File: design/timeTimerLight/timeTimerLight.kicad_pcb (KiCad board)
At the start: 2 copper layers, 1 part

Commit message: Got components layed out on PCB editor, no traces yet.  Switched to right-angle connector.
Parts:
- removed REF**: MCP1640, Package_TO_SOT_SMD:SOT-23-6
- added C1: 10u, customParts:CAPRB250W50L400T250H550, F.Cu at (138.0, 116.0)
- added C2: 10u, customParts:CAPRB250W50L400T250H550, F.Cu at (156.5, 120.5)
- added D1: LED, LED_THT:LED_D5.0mm, F.Cu at (162.5, 135.0)
- added J1: 640455-3, customParts:TE_640455-3, F.Cu at (127.4, 120.3)
- added L1: 4u7, customParts:IND_CDRH2D18_HPNP-4R7NC, F.Cu at (139.5, 128.0)
- added Q1: 2N3906, Package_TO_SOT_THT:TO-92_Inline, F.Cu at (149.1, 115.2)
- added R1: 10k, customParts:RESAD1100W55L630D240B, F.Cu at (138.5, 120.5)
- added R2: 100k, customParts:RESAD1100W55L630D240B, F.Cu at (132.5, 130.5)
- added R3: 976k, customParts:RESAD1100W55L630D240B, F.Cu at (150.0, 126.0)
- added R4: 562k, customParts:RESAD1100W55L630D240B, F.Cu at (150.0, 129.5)
- added R5: 220R, customParts:RESAD1100W55L630D240B, F.Cu at (163.0, 121.0)
- added S1: OS102011MS2QS1, customParts:OS102011MS2QS1, F.Cu at (123.5, 128.6)
- added U1: MCP1640x-xCHY, Package_TO_SOT_SMD:SOT-23-6, F.Cu at (142.0, 134.0)
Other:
- board outline added: 50.8 x 25.4 mm

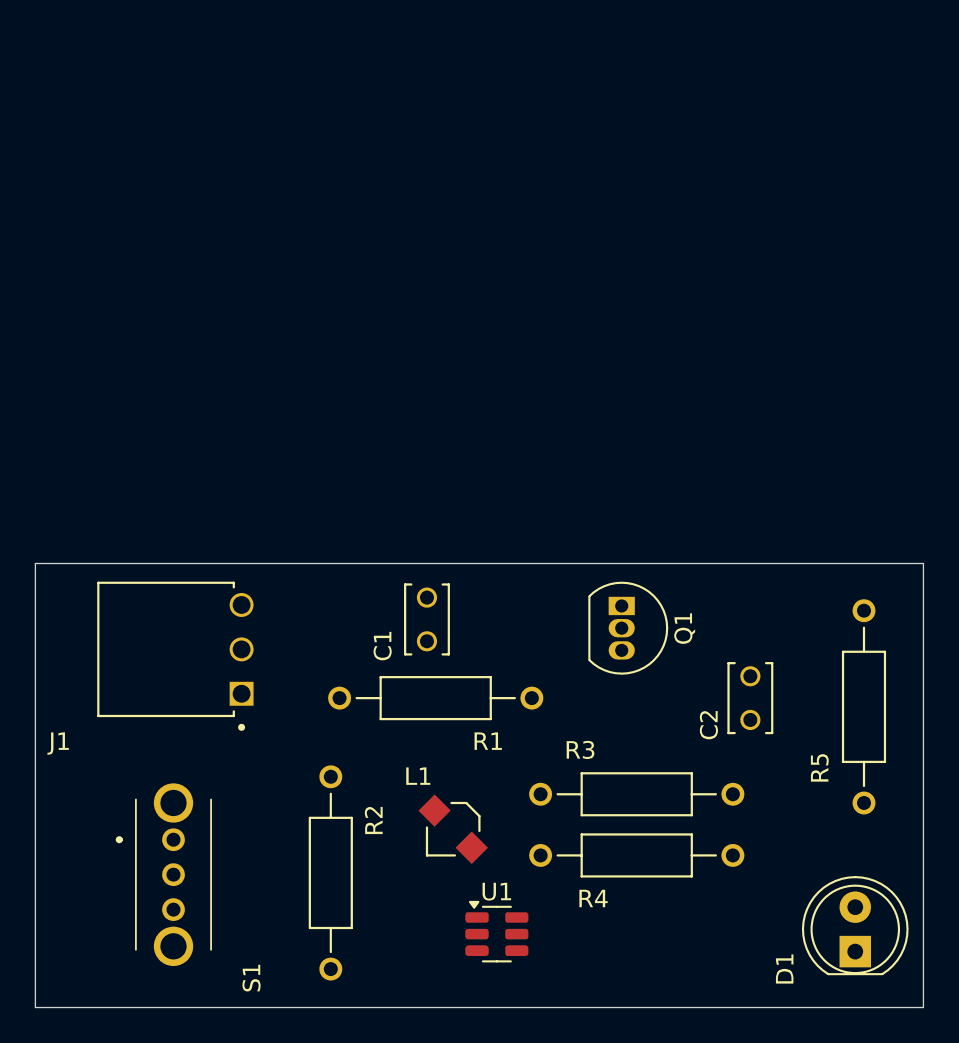
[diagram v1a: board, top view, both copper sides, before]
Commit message: Front traces done.  Still need to do ground plane
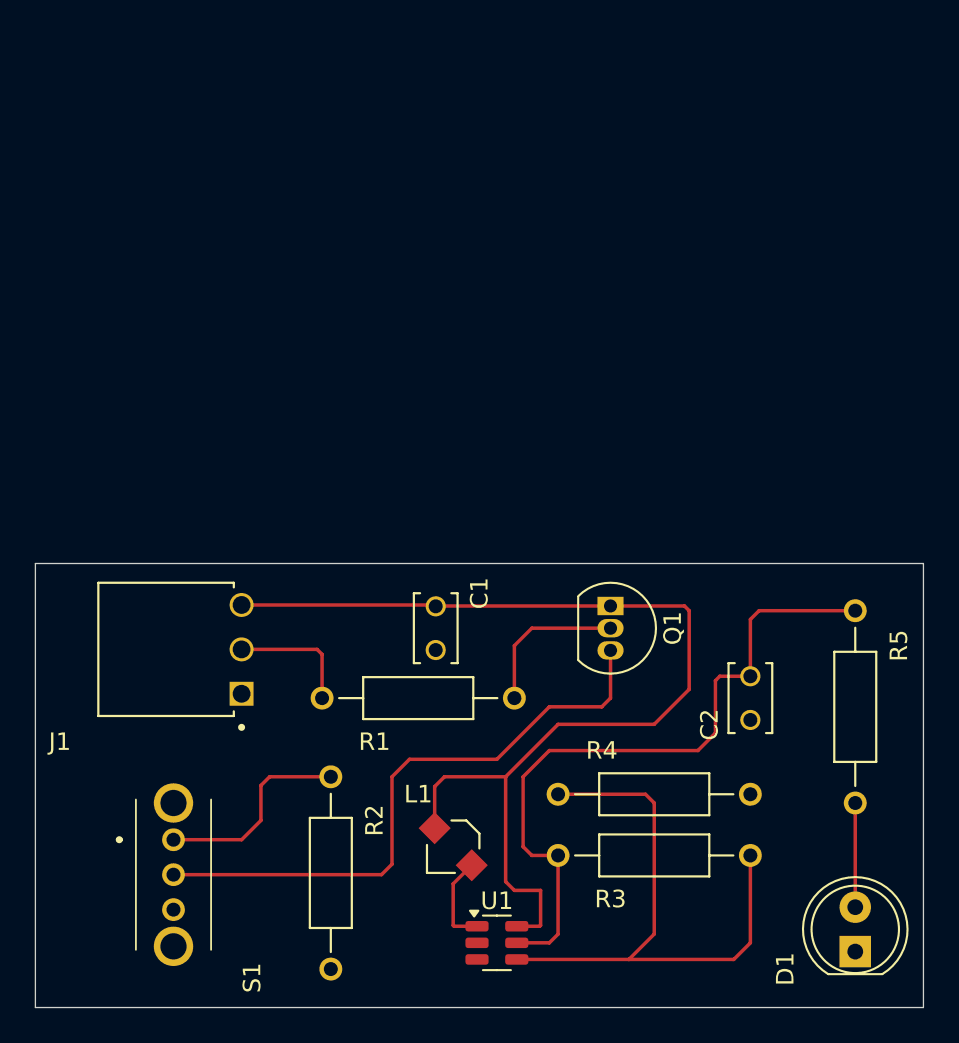
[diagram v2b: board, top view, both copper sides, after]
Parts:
- moved R3 3.64 mm to (151.0, 129.5)
- moved R4 3.64 mm to (151.0, 126.0)
- moved L1 1.00 mm to (139.5, 129.0)
- moved R1 1.00 mm to (137.5, 120.5), turned to 180 degrees
- moved C1 0.71 mm to (138.5, 116.5), turned to -90 degrees
- moved Q1 0.64 mm to (148.5, 115.2)
- moved R5 0.50 mm to (162.5, 121.0), turned to -90 degrees
- moved U1 0.50 mm to (142.0, 134.5)
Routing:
- net /+1V2: track 0.00 -> 61.1 mm
- net GND1: track 0.00 -> 39.9 mm
- net Net-(Q1-C): track 0.00 -> 34.8 mm
- net Net-(U1-V_{FB}): track 0.00 -> 34.0 mm
- net Net-(S1-NO): track 0.00 -> 11.7 mm
- net Net-(Q1-B): track 0.00 -> 8.91 mm
- net /ALARM: track 0.00 -> 7.22 mm
- net Net-(D1-A): track 0.00 -> 5.96 mm
- net Net-(U1-SW): track 0.00 -> 5.26 mm

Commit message: Back ground traces done too
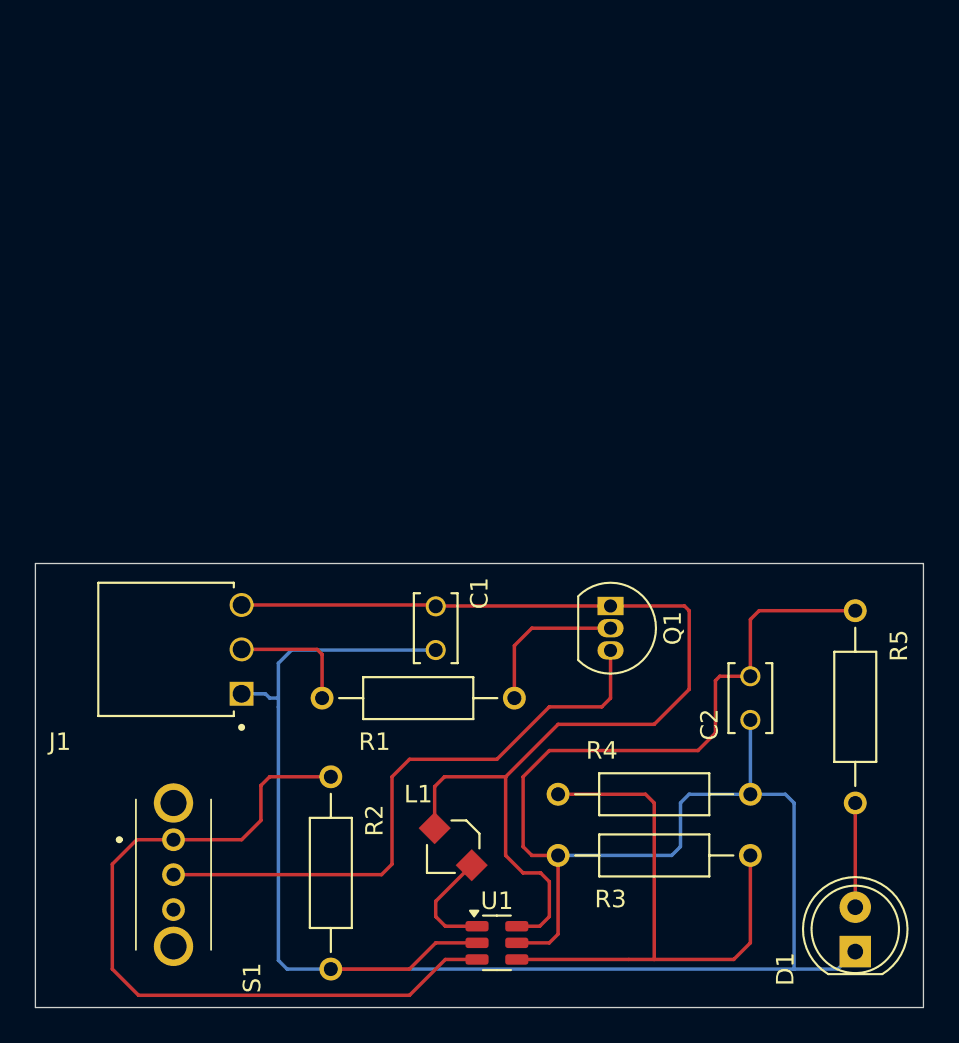
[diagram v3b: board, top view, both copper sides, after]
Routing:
- net GND1: track 39.9 -> 138.9 mm
- net Net-(S1-NO): track 11.7 -> 44.1 mm
- net Net-(U1-SW): track 5.26 -> 6.38 mm
- net Net-(U1-V_{FB}): track 34.0 -> 33.4 mm
